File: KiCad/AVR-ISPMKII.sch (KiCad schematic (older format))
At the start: 31 parts, among them J1 USB_C_Receptacle_USB2.0, J2 Self_Program, J3 V_Target, J4 ISP_Header, U1 ATmega16U2-MU, U2 AP7365-33WG-7, U3 NLSX4373DMR2G, Y1 16MHz

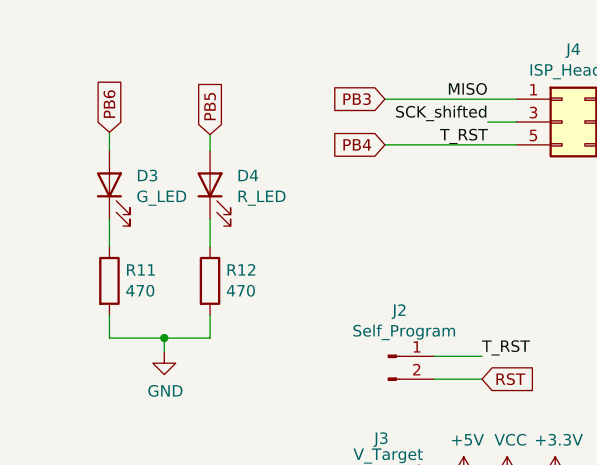
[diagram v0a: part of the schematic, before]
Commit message: Updated LED resistors, corrected .gitignore
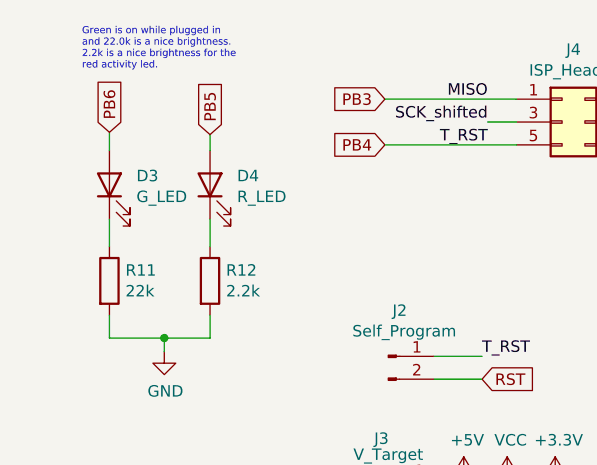
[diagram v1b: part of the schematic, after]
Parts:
- R11: value 470 -> 22k
- R12: value 470 -> 2.2k
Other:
- note added: "Green is on while plugged in\nand 22.0k is a nice brightness.\n2.2k is a nice brightness for the\nred activity led."
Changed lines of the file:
@@
 P 920 1620
 F 0 "R11" H 990 1666 50  0000 L CNN
-F 1 "470" H 990 1575 50  0000 L CNN
+F 1 "22k" H 990 1575 50  0000 L CNN
 F 2 "Resistor_SMD:R_0603_1608Metric" V 850 1620 50  0001 C CNN
 F 3 "~" H 920 1620 50  0001 C CNN
@@
 P 1360 1620
 F 0 "R12" H 1430 1666 50  0000 L CNN
-F 1 "470" H 1430 1575 50  0000 L CNN
+F 1 "2.2k" H 1430 1575 50  0000 L CNN
 F 2 "Resistor_SMD:R_0603_1608Metric" V 1290 1620 50  0001 C CNN
 F 3 "~" H 1360 1620 50  0001 C CNN
@@
 Wire Wire Line
 	5000 1200 5000 1450
+Text Notes 800  700  0    31   ~ 0
+Green is on while plugged in\nand 22.0k is a nice brightness.\n2.2k is a nice brightness for the\nred activity led.
 $EndSCHEMATC

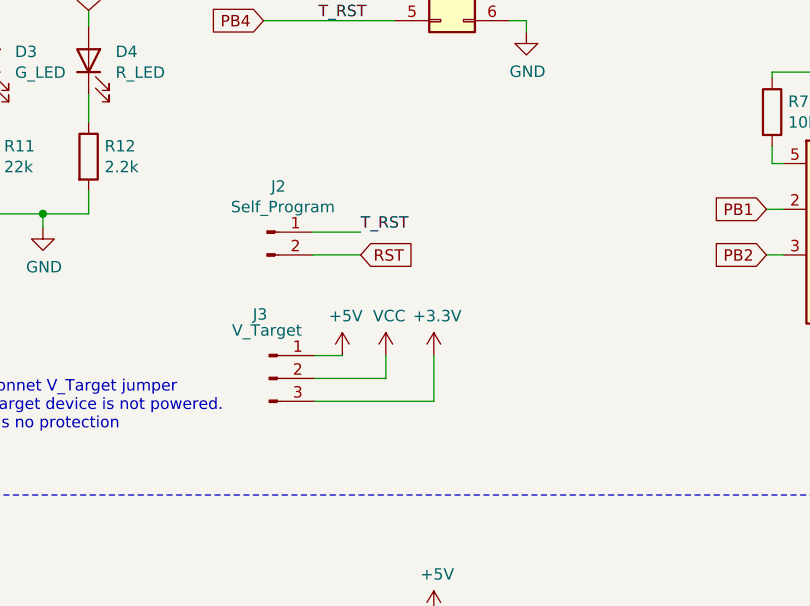
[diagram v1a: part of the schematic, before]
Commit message: Updated USB trace
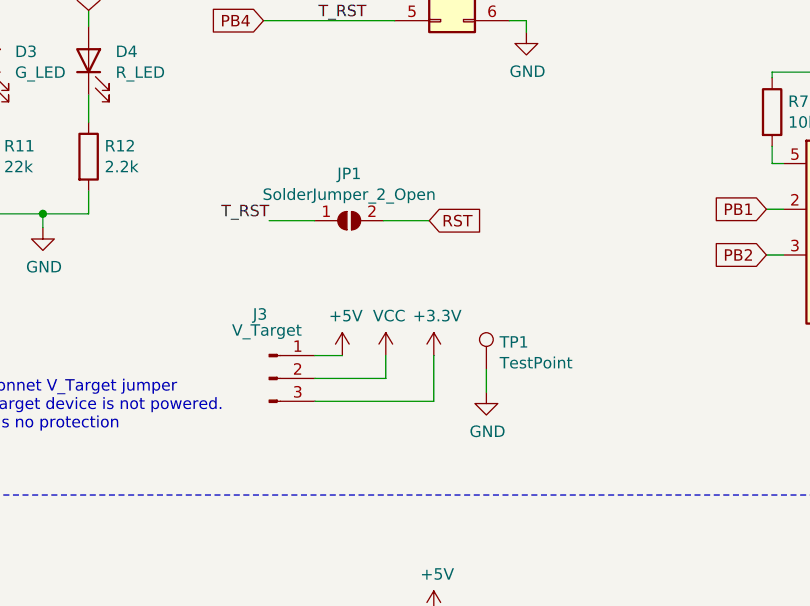
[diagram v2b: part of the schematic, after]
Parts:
- removed J2: Self_Program, Connector_PinHeader_2.54mm:PinHeader_1x02_P2.54mm_Vertical, symbol AVR-ISPMKII-rescue:Conn_01x02_Male-Connector
- added JP1: SolderJumper_2_Open, Jumper:SolderJumper-2_P1.3mm_Open_TrianglePad1.0x1.5mm, symbol Jumper:SolderJumper_2_Open
- added TP1: TestPoint, TestPoint:TestPoint_Pad_D2.0mm, symbol Connector:TestPoint
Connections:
- net GND: now also TP1.1
- net PB4: now also JP1.1 (A)
- net RST: now also JP1.2 (B)
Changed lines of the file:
@@
 	1    0    0    -1
 $EndComp
-$Comp
-L AVR-ISPMKII-rescue:Conn_01x02_Male-Connector J2
-U 1 1 60D064F3
-P 2140 1950
-F 0 "J2" H 2190 2150 50  0000 C CNN
-F 1 "Self_Program" H 2210 2060 50  0000 C CNN
-F 2 "Connector_PinHeader_2.54mm:PinHeader_1x02_P2.54mm_Vertical" H 2140 1950 50  0001 C CNN
-F 3 "~" H 2140 1950 50  0001 C CNN
-	1    2140 1950
-	1    0    0    -1
-$EndComp
-Text GLabel 2550 2050 2    50   Input ~ 0
+Text GLabel 2850 1900 2    50   Input ~ 0
 RST
-Text Label 2550 1950 0    50   ~ 0
-T_RST
-Wire Wire Line
-	2550 1950 2340 1950
-Wire Wire Line
-	2340 2050 2550 2050
 $Comp
 L AVR-ISPMKII-rescue:C-Device C6
@@
 Text Notes 800  700  0    31   ~ 0
 Green is on while plugged in\nand 22.0k is a nice brightness.\n2.2k is a nice brightness for the\nred activity led.
+$Comp
+L Jumper:SolderJumper_2_Open JP1
+U 1 1 612EE5CA
+P 2500 1900
+F 0 "JP1" H 2500 2105 50  0000 C CNN
+F 1 "SolderJumper_2_Open" H 2500 2014 50  0000 C CNN
+F 2 "Jumper:SolderJumper-2_P1.3mm_Open_TrianglePad1.0x1.5mm" H 2500 1900 50  0001 C CNN
+F 3 "~" H 2500 1900 50  0001 C CNN
+	1    2500 1900
+	1    0    0    -1
+$EndComp
+Text Label 2150 1900 2    50   ~ 0
+T_RST
+Wire Wire Line
+	2350 1900 2150 1900
+Wire Wire Line
+	2850 1900 2650 1900
+$Comp
+L Connector:TestPoint TP1
+U 1 1 6132262D
+P 3100 2550
+F 0 "TP1" H 3158 2668 50  0000 L CNN
+F 1 "TestPoint" H 3158 2577 50  0000 L CNN
+F 2 "TestPoint:TestPoint_Pad_D2.0mm" H 3300 2550 50  0001 C CNN
+F 3 "~" H 3300 2550 50  0001 C CNN
+	1    3100 2550
+	1    0    0    -1
+$EndComp
+$Comp
+L AVR-ISPMKII-rescue:GND-power #PWR0105
+U 1 1 6132377A
+P 3100 2650
+F 0 "#PWR0105" H 3100 2400 50  0001 C CNN
+F 1 "GND" H 3105 2477 50  0000 C CNN
+F 2 "" H 3100 2650 50  0001 C CNN
+F 3 "" H 3100 2650 50  0001 C CNN
+	1    3100 2650
+	1    0    0    -1
+$EndComp
+Wire Wire Line
+	3100 2550 3100 2650
 $EndSCHEMATC
